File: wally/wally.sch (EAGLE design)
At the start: 108 parts, among them IC1 ESP32-S3-WROOM-1U-N16, IC2 XTLV61048DBVR, IC3 TLV1117LV33DCYR, IC4 DPS310XTSA1, IC5 MS560702BA03-50, IC6 LSM6DSV16BXTR, IC7 MLX90395KLW-BBA-001-SP, J1 MSD-4-A, J2 QWIIC_RIGHT_ANGLE, J3 QWIIC_RIGHT_ANGLE, J5 USB4105-GF-A, U1 RA-01H

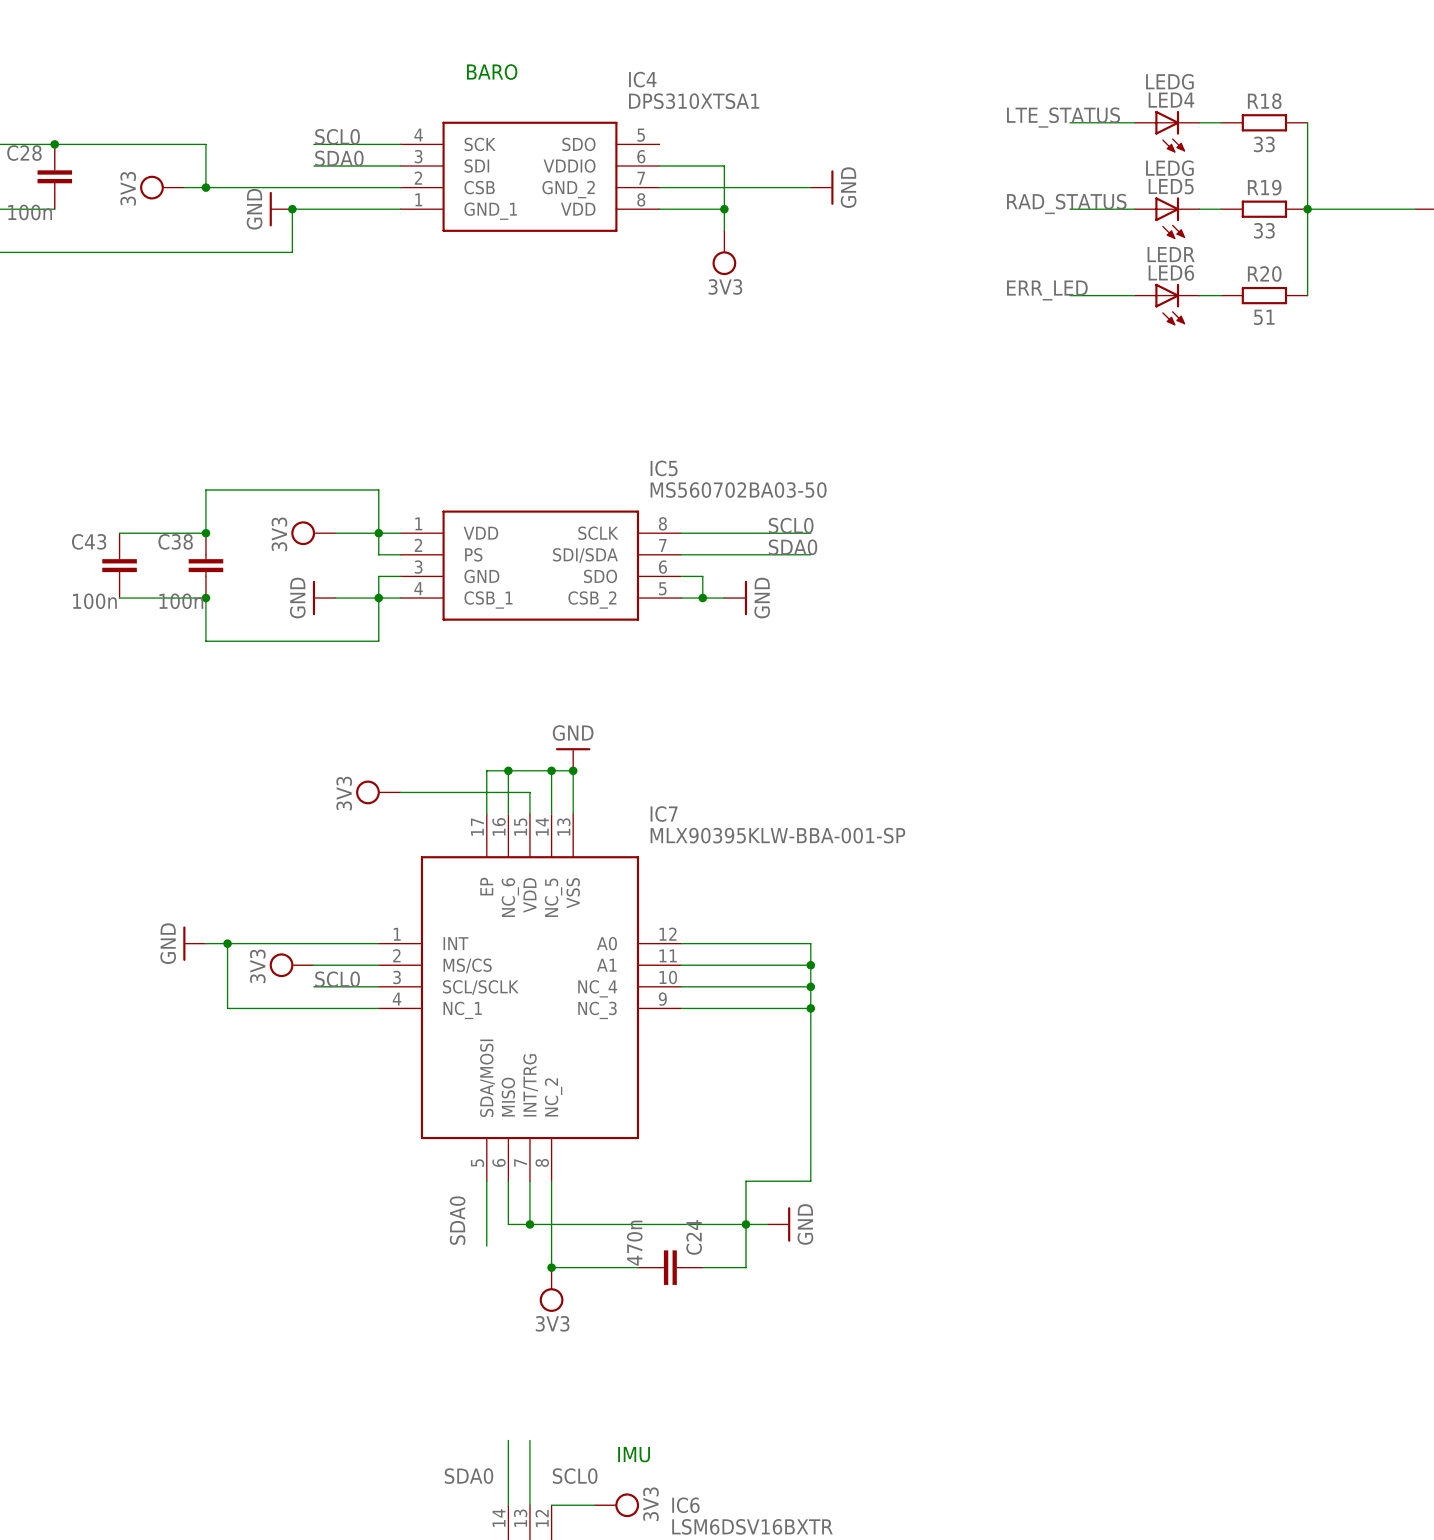
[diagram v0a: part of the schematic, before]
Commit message: swap mag IC
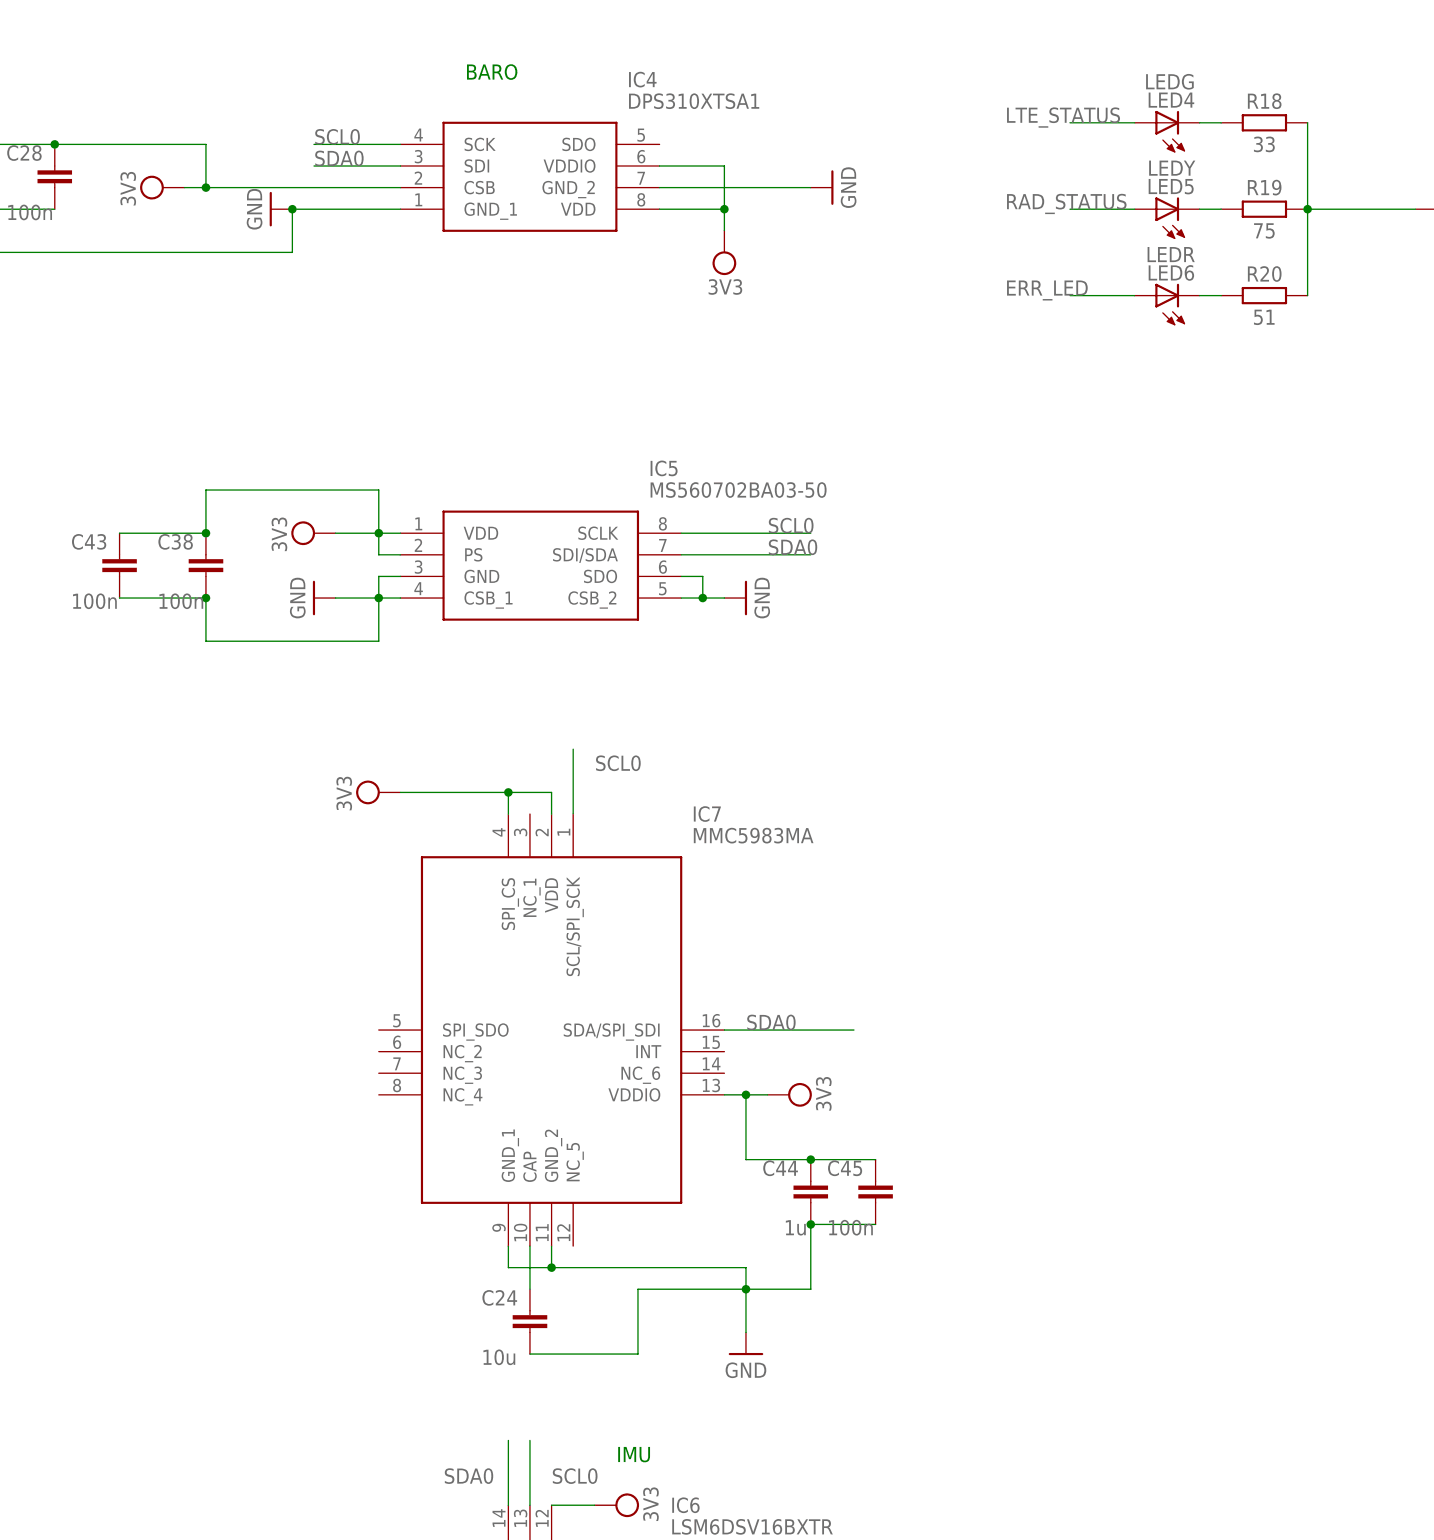
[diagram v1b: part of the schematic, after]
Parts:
- added C44: 1u, Capacitor:C_CHIP-0402(1005-METRIC)
- added C45: 100n, Capacitor:C_CHIP-0402(1005-METRIC)
- C24: value 470n -> 10u; device Capacitor:C_CHIP-0603(1608-METRIC) -> Capacitor:C_CHIP-0402(1005-METRIC)
- IC7: value MLX90395KLW-BBA-001-SP -> MMC5983MA; device SamacSys_Parts:MLX90395KLW-BBA-001-SP -> SamacSys_Parts:MMC5983MA
- LED5: value LEDG -> LEDY
- R19: value 33 -> 75; device Resistor:R_CHIP-0402(1005-METRIC) -> Resistor:R_CHIP-0603(1608-METRIC)
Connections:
- new net N$6: C24.1, IC7.CAP
- net 3V3: now also C44.1, C45.1, IC7.SPI_CS, IC7.VDDIO; no longer C24.2, IC7.MS/CS, IC7.NC_2
- net GND: now also C24.2, C44.2, C45.2, IC7.GND_1, IC7.GND_2; no longer C24.1, IC7.A0, IC7.A1, IC7.EP, IC7.INT, IC7.INT/TRG, IC7.MISO, IC7.NC_1, IC7.NC_3, IC7.NC_4, IC7.NC_5, IC7.NC_6, IC7.VSS
- net SCL0: now also IC7.SCL/SPI_SCK; no longer IC7.SCL/SCLK
- net SDA0: now also IC7.SDA/SPI_SDI; no longer IC7.SDA/MOSI
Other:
- moved on the sheet: C24

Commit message: add gpio connector
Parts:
- removed TP14, TP15: PTR1B2,54, testpad:PTR1B2,54
- added J4: SM06B-SRSS-TB__LF__SN_, SamacSys_Parts:SM06B-SRSS-TB__LF__SN_
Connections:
- removed net ERR_LED: IC1.IO8, LED6.A
- removed net LTE_STATUS: IC1.IO9, LED4.A
- removed net RAD_STATUS: IC1.IO10, LED5.A
- new net A2: IC1.IO10, J4.4, LED4.A
- new net A3: IC1.IO6, J4.5
- new net A4: IC1.IO16, J4.6
- net A0: now also IC1.IO8, J4.2, LED6.A; no longer IC1.IO6, TP15.TP
- net A1: now also IC1.IO9, J4.3, LED5.A; no longer IC1.IO16, TP14.TP
- net GND: now also J4.1
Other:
- note added: "HR_ACC"
- note added: "HR_BARO"
- note added: "MAG"

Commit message: swap hr baro with bme
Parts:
- removed C38, C43: 100n, Capacitor:C_CHIP-0402(1005-METRIC)
- removed IC5: MS560702BA03-50, SamacSys_Parts:MS560702BA03-50
- added IC9: BME688, SamacSys_Parts:BME688
- added J6: FEMALE 2x3, SparkFun-Connectors:CONN_03X2FEMALE
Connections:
- net 3V3: now also IC4.SDO; no longer C38.1, C43.1, IC5.PS, IC5.VDD
- net A0: now also J6.2
- net A1: now also J6.4
- net A2: now also J6.6
- net A3: now also J6.3
- net A4: now also J6.5
- net GND: now also J6.1; no longer C38.2, C43.2, IC5.CSB_1, IC5.CSB_2, IC5.GND, IC5.SDO
- net SCL0: no longer IC5.SCLK, IC7.SCL/SPI_SCK
- net SDA0: no longer IC5.SDI/SDA
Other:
- note removed: "HR_BARO"

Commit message: swap to dps368
dps310 is nrnd
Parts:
- added C46: 1u, Capacitor:C_CHIP-0402(1005-METRIC)
- added IC8: APDS-9253-001, SamacSys_Parts:APDS-9253-001
- IC4: value DPS310XTSA1 -> DPS368XTSA1; device SamacSys_Parts:DPS310XTSA1 -> SamacSys_Parts:DPS368XTSA1

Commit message: change i2c pullup vals
move to 5k1 from 10k
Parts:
- added C38, C43: 100n, Capacitor:C_CHIP-0402(1005-METRIC)
- R5, R6, R7, R8: value 10k -> 5k1
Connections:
- net 3V3: now also C38.1, C43.1, C46.1, IC8.VDD, IC9.CSB, IC9.VDD, IC9.VDDIO
- net GND: now also C38.2, C43.2, C46.2, IC8.GND, IC9.GND_1, IC9.GND_2, IC9.SDO
- net SCL0: now also IC8.SCL, IC9.SCK
- net SDA0: now also IC8.SDA, IC9.SDI
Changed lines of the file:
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@@
 <part name="SUPPLY29" library="Power_Symbols" library_urn="urn:adsk.eagle:library:16502351" deviceset="GND-BAR" device="" value="GND"/>
 <part name="SUPPLY30" library="Power_Symbols" library_urn="urn:adsk.eagle:library:16502351" deviceset="3V3-CIRCLE" device="" value="3V3"/>
-<part name="R5" library="Resistor" library_urn="urn:adsk.eagle:library:16378527" deviceset="R" device="CHIP-0402(1005-METRIC)" package3d_urn="urn:adsk.eagle:package:16378568/5" technology="_" value="10k"/>
-<part name="R6" library="Resistor" library_urn="urn:adsk.eagle:library:16378527" deviceset="R" device="CHIP-0402(1005-METRIC)" package3d_urn="urn:adsk.eagle:package:16378568/5" technology="_" value="10k"/>
-<part name="R7" library="Resistor" library_urn="urn:adsk.eagle:library:16378527" deviceset="R" device="CHIP-0402(1005-METRIC)" package3d_urn="urn:adsk.eagle:package:16378568/5" technology="_" value="10k"/>
-<part name="R8" library="Resistor" library_urn="urn:adsk.eagle:library:16378527" deviceset="R" device="CHIP-0402(1005-METRIC)" package3d_urn="urn:adsk.eagle:package:16378568/5" technology="_" value="10k"/>
+<part name="R5" library="Resistor" library_urn="urn:adsk.eagle:library:16378527" deviceset="R" device="CHIP-0402(1005-METRIC)" package3d_urn="urn:adsk.eagle:package:16378568/5" technology="_" value="5k1"/>
+<part name="R6" library="Resistor" library_urn="urn:adsk.eagle:library:16378527" deviceset="R" device="CHIP-0402(1005-METRIC)" package3d_urn="urn:adsk.eagle:package:16378568/5" technology="_" value="5k1"/>
+<part name="R7" library="Resistor" library_urn="urn:adsk.eagle:library:16378527" deviceset="R" device="CHIP-0402(1005-METRIC)" package3d_urn="urn:adsk.eagle:package:16378568/5" technology="_" value="5k1"/>
+<part name="R8" library="Resistor" library_urn="urn:adsk.eagle:library:16378527" deviceset="R" device="CHIP-0402(1005-METRIC)" package3d_urn="urn:adsk.eagle:package:16378568/5" technology="_" value="5k1"/>
 <part name="SUPPLY32" library="Power_Symbols" library_urn="urn:adsk.eagle:library:16502351" deviceset="3V3-CIRCLE" device="" value="3V3"/>
 <part name="D2" library="SamacSys_Parts" deviceset="SSA34-E3_5AT" device="" override_package3d_urn="urn:adsk.eagle:package:44099325/2" override_package_urn="urn:adsk.eagle:footprint:44099326/1"/>
@@
 <part name="SUPPLY31" library="Power_Symbols" library_urn="urn:adsk.eagle:library:16502351" deviceset="GND-BAR" device="" value="GND"/>
 <part name="SUPPLY51" library="Power_Symbols" library_urn="urn:adsk.eagle:library:16502351" deviceset="GND-BAR" device="" value="GND"/>
+<part name="SUPPLY52" library="Power_Symbols" library_urn="urn:adsk.eagle:library:16502351" deviceset="3V3-CIRCLE" device="" value="3V3"/>
+<part name="C38" library="Capacitor" library_urn="urn:adsk.eagle:library:16290819" deviceset="C" device="CHIP-0402(1005-METRIC)" package3d_urn="urn:adsk.eagle:package:16290895/5" technology="_" value="100n"/>
+<part name="C43" library="Capacitor" library_urn="urn:adsk.eagle:library:16290819" deviceset="C" device="CHIP-0402(1005-METRIC)" package3d_urn="urn:adsk.eagle:package:16290895/5" technology="_" value="100n"/>
 </parts>
 <sheets>
@@
 <instance part="SUPPLY51" gate="G$1" x="-50.8" y="-233.68" smashed="yes" rot="MR0">
 <attribute name="VALUE" x="-50.8" y="-235.585" size="1.778" layer="96" rot="MR0" align="center"/>
+</instance>
+<instance part="SUPPLY52" gate="G$1" x="55.88" y="-670.56" smashed="yes" rot="R270">
+<attribute name="VALUE" x="59.055" y="-670.433" size="1.778" layer="96" rot="R270" align="bottom-center"/>
+</instance>
+<instance part="C38" gate="G$1" x="5.08" y="-660.4" smashed="yes" rot="R180">
+<attribute name="NAME" x="10.795" y="-661.035" size="1.778" layer="95" rot="R180"/>
+<attribute name="VALUE" x="10.795" y="-654.05" size="1.778" layer="96" rot="R180"/>
+</instance>
+<instance part="C43" gate="G$1" x="12.7" y="-660.4" smashed="yes" rot="R180">
+<attribute name="NAME" x="18.415" y="-661.035" size="1.778" layer="95" rot="R180"/>
+<attribute name="VALUE" x="18.415" y="-654.05" size="1.778" layer="96" rot="R180"/>
 </instance>
 </instances>
@@
 <junction x="-50.8" y="-226.06"/>
 </segment>
+<segment>
+<pinref part="IC8" gate="G$1" pin="GND"/>
+<pinref part="SUPPLY40" gate="G$1" pin="GND"/>
+<wire x1="30.48" y1="-632.46" x2="38.1" y2="-632.46" width="0.1524" layer="91"/>
+<pinref part="C46" gate="G$1" pin="2"/>
+<wire x1="38.1" y1="-632.46" x2="43.18" y2="-632.46" width="0.1524" layer="91"/>
+<wire x1="22.86" y1="-647.7" x2="38.1" y2="-647.7" width="0.1524" layer="91"/>
+<wire x1="38.1" y1="-647.7" x2="38.1" y2="-632.46" width="0.1524" layer="91"/>
+<junction x="38.1" y="-632.46"/>
+</segment>
+<segment>
+<pinref part="IC9" gate="G$1" pin="GND_2"/>
+<pinref part="SUPPLY55" gate="G$1" pin="GND"/>
+<wire x1="2.54" y1="-670.56" x2="-5.08" y2="-670.56" width="0.1524" layer="91"/>
+<pinref part="IC9" gate="G$1" pin="SDO"/>
+<wire x1="-5.08" y1="-670.56" x2="-12.7" y2="-670.56" width="0.1524" layer="91"/>
+<wire x1="2.54" y1="-675.64" x2="-5.08" y2="-675.64" width="0.1524" layer="91"/>
+<wire x1="-5.08" y1="-675.64" x2="-5.08" y2="-670.56" width="0.1524" layer="91"/>
+<junction x="-5.08" y="-670.56"/>
+</segment>
+<segment>
+<pinref part="SUPPLY54" gate="G$1" pin="GND"/>
+<pinref part="IC9" gate="G$1" pin="GND_1"/>
+<wire x1="43.18" y1="-668.02" x2="38.1" y2="-668.02" width="0.1524" layer="91"/>
+<pinref part="C38" gate="G$1" pin="2"/>
+<pinref part="C43" gate="G$1" pin="2"/>
+<wire x1="38.1" y1="-668.02" x2="33.02" y2="-668.02" width="0.1524" layer="91"/>
+<wire x1="5.08" y1="-655.32" x2="12.7" y2="-655.32" width="0.1524" layer="91"/>
+<wire x1="12.7" y1="-655.32" x2="38.1" y2="-655.32" width="0.1524" layer="91"/>
+<wire x1="38.1" y1="-655.32" x2="38.1" y2="-668.02" width="0.1524" layer="91"/>
+<junction x="12.7" y="-655.32"/>
+<junction x="38.1" y="-668.02"/>
+</segment>
 </net>
 <net name="3V3" class="0">
@@
 <pinref part="IC4" gate="G$1" pin="CSB"/>
 <wire x1="35.56" y1="-220.98" x2="25.4" y2="-220.98" width="0.1524" layer="91"/>
+</segment>
+<segment>
+<pinref part="SUPPLY57" gate="G$1" pin="3V3"/>
+<pinref part="IC8" gate="G$1" pin="VDD"/>
+<wire x1="-2.54" y1="-637.54" x2="0" y2="-637.54" width="0.1524" layer="91"/>
+<pinref part="C46" gate="G$1" pin="1"/>
+<wire x1="0" y1="-637.54" x2="5.08" y2="-637.54" width="0.1524" layer="91"/>
+<wire x1="15.24" y1="-647.7" x2="0" y2="-647.7" width="0.1524" layer="91"/>
+<wire x1="0" y1="-647.7" x2="0" y2="-637.54" width="0.1524" layer="91"/>
+<junction x="0" y="-637.54"/>
+</segment>
+<segment>
+<pinref part="IC9" gate="G$1" pin="VDD"/>
+<pinref part="SUPPLY56" gate="G$1" pin="3V3"/>
+<wire x1="2.54" y1="-668.02" x2="-2.54" y2="-668.02" width="0.1524" layer="91"/>
+<pinref part="IC9" gate="G$1" pin="VDDIO"/>
+<wire x1="-2.54" y1="-668.02" x2="-5.08" y2="-668.02" width="0.1524" layer="91"/>
+<wire x1="2.54" y1="-673.1" x2="-2.54" y2="-673.1" width="0.1524" layer="91"/>
+<wire x1="-2.54" y1="-673.1" x2="-2.54" y2="-668.02" width="0.1524" layer="91"/>
+<junction x="-2.54" y="-668.02"/>
+<wire x1="-2.54" y1="-668.02" x2="-2.54" y2="-662.94" width="0.1524" layer="91"/>
+<pinref part="C38" gate="G$1" pin="1"/>
+<wire x1="-2.54" y1="-662.94" x2="5.08" y2="-662.94" width="0.1524" layer="91"/>
+<pinref part="C43" gate="G$1" pin="1"/>
+<wire x1="5.08" y1="-662.94" x2="12.7" y2="-662.94" width="0.1524" layer="91"/>
+<junction x="5.08" y="-662.94"/>
+</segment>
+<segment>
+<pinref part="SUPPLY52" gate="G$1" pin="3V3"/>
+<pinref part="IC9" gate="G$1" pin="CSB"/>
+<wire x1="53.34" y1="-670.56" x2="33.02" y2="-670.56" width="0.1524" layer="91"/>
 </segment>
 </net>
@@
 <label x="35.56" y="-322.58" size="1.778" layer="95"/>
 </segment>
+<segment>
+<pinref part="IC8" gate="G$1" pin="SDA"/>
+<wire x1="5.08" y1="-635" x2="-15.24" y2="-635" width="0.1524" layer="91"/>
+<label x="-15.24" y="-635" size="1.778" layer="95"/>
+</segment>
+<segment>
+<pinref part="IC9" gate="G$1" pin="SDI"/>
+<wire x1="33.02" y1="-673.1" x2="48.26" y2="-673.1" width="0.1524" layer="91"/>
+<label x="48.26" y="-673.1" size="1.778" layer="95"/>
+</segment>
 </net>
 <net name="USB_P" class="0">
@@
 <label x="-20.32" y="-477.52" size="1.778" layer="95"/>
 </segment>
+<segment>
+<pinref part="IC8" gate="G$1" pin="SCL"/>
+<wire x1="5.08" y1="-632.46" x2="-15.24" y2="-632.46" width="0.1524" layer="91"/>
+<label x="-15.24" y="-632.46" size="1.778" layer="95"/>
+</segment>
+<segment>
+<pinref part="IC9" gate="G$1" pin="SCK"/>
+<wire x1="33.02" y1="-675.64" x2="48.26" y2="-675.64" width="0.1524" layer="91"/>
+<label x="48.26" y="-675.64" size="1.778" layer="95"/>
+</segment>
 </net>

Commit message: route new i2c traces
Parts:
- removed J4: SM06B-SRSS-TB__LF__SN_, SamacSys_Parts:SM06B-SRSS-TB__LF__SN_
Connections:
- net A0: no longer J4.2
- net A1: no longer J4.3
- net A2: no longer J4.4
- net A3: no longer J4.5
- net A4: no longer J4.6
- net GND: no longer J4.1
- net SCL0: now also IC7.SCL/SPI_SCK
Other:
- moved on the sheet: C38, C43, C46, IC8, IC9

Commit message: export new wally
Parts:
- J6: device SparkFun-Connectors:CONN_03X2FEMALE -> SparkFun-Connectors:CONN_03X2NO_SILK
